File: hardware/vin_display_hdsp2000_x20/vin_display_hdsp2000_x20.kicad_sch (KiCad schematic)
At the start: 51 parts, among them J1 DEBUG, J2 USB_B_Micro, J3 DEBUG_UART, J4 IF_UART, J5 AUX_CONNECTOR, Q1 BSS138, SW1 SW_RESET, SW2 BOOTSEL, SW3 KNOB, U1 W25Q16JVSNIQ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

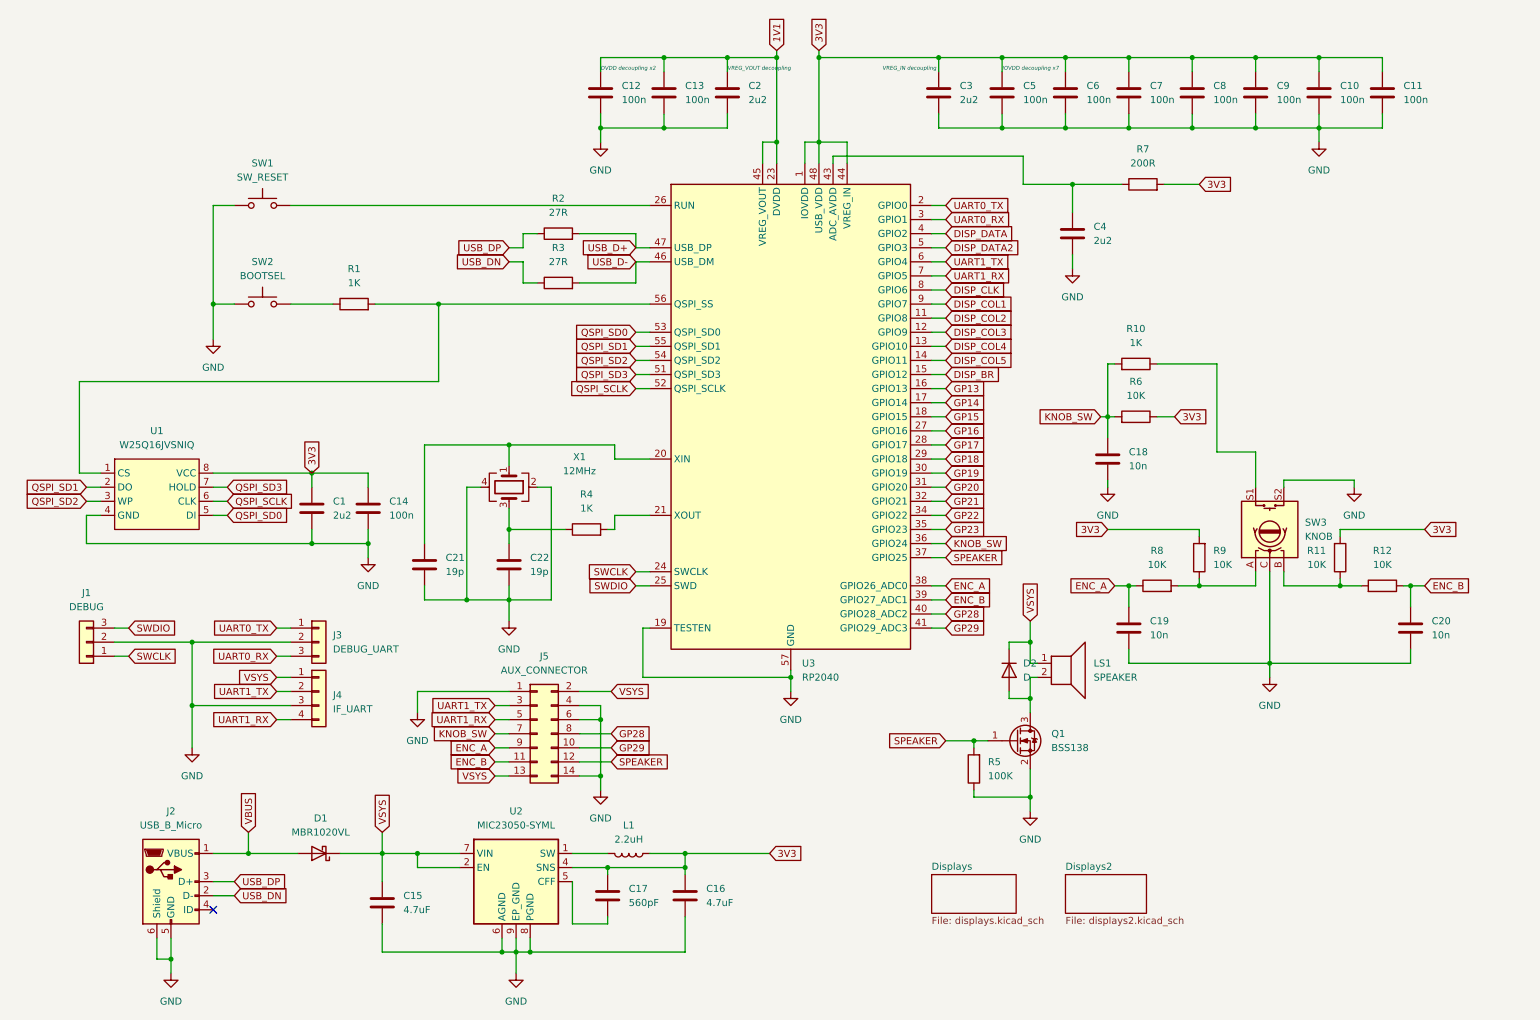
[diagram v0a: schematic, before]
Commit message: route hdsp2000_x20 board
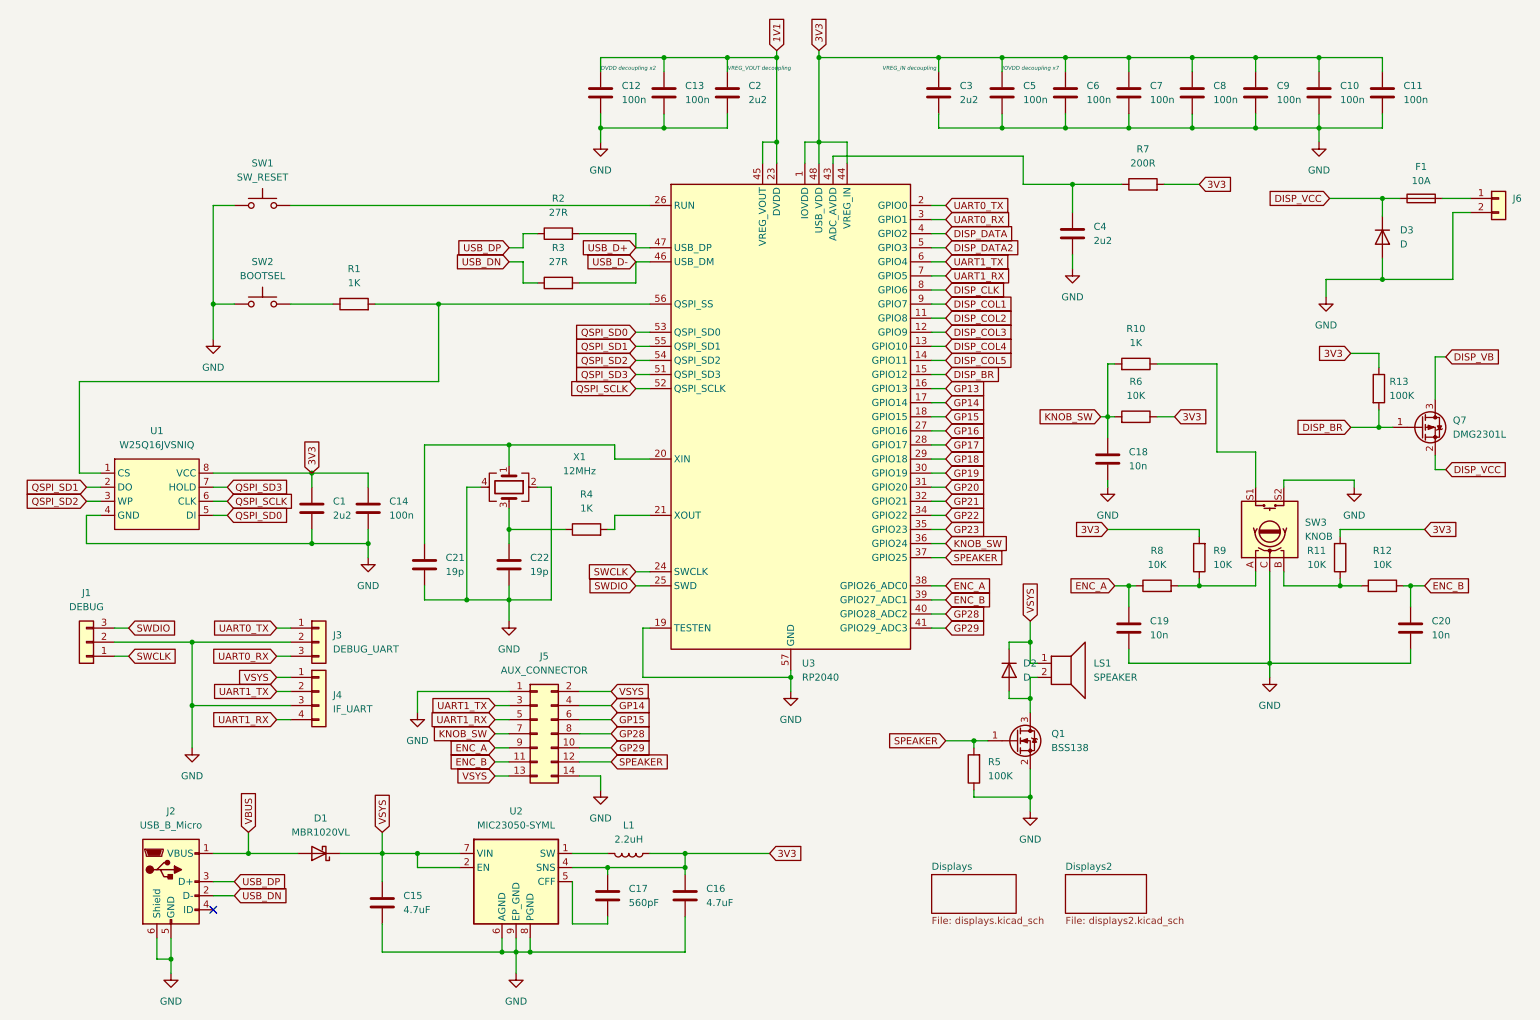
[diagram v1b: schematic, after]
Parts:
- added D3: D, components:Diode_TO252, symbol Device:D
- added F1: 10A, components:Fuse_2410, symbol Device:Fuse
- added J6: Conn_01x02, components:Conn_2x3_96, symbol Connector_Generic:Conn_01x02
- added Q7: DMG2301L, Package_TO_SOT_SMD:SOT-23, symbol Transistor_FET:DMG2301L
- added R13: 100K, Resistor_SMD:R_0603_1608Metric, symbol Device:R
- J1, J3: footprint Connector_PinHeader_2.54mm:PinHeader_1x03_P2.54mm_Vertical -> Connector_JST:JST_EH_B3B-EH-A_1x03_P2.50mm_Vertical
- J4: footprint Connector_PinHeader_2.54mm:PinHeader_1x04_P2.54mm_Vertical -> Connector_JST:JST_EH_B4B-EH-A_1x04_P2.50mm_Vertical
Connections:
- net 3V3: now also R13.1
- net DISP_BR: now also Q7.1 (G), R13.2
- net GND: now also D3.2 (A), J6.2 (Pin_2); no longer J5.4 (Pin_4), J5.6 (Pin_6)
- net GP14: now also J5.4 (Pin_4)
- net GP15: now also J5.6 (Pin_6)
- new net: F1.2, J6.1 (Pin_1)
- new net DISP_VB: Q7.3 (D)
- new net DISP_VCC: D3.1 (K), F1.1, Q7.2 (S)

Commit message: hdsp2000_x20 minor changes
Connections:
- net GP13: no longer names the net of U3.16 (GPIO13)
- net GP16: no longer names the net of U3.27 (GPIO16)
- net GP17: no longer names the net of U3.28 (GPIO17)
- net GP18: no longer names the net of U3.29 (GPIO18)
- net GP19: no longer names the net of U3.30 (GPIO19)
- net GP20: no longer names the net of U3.31 (GPIO20)
- net GP21: no longer names the net of U3.32 (GPIO21)
- net GP22: no longer names the net of U3.34 (GPIO22)
- net GP23: no longer names the net of U3.35 (GPIO23)
- no-connect marks 1 -> 10
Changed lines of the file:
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@@
   (junction (at 130.81 22.86) (diameter 0) (color 0 0 0 0)
   )
+  (no_connect (at 181.61 97.79))
+  (no_connect (at 181.61 90.17))
+  (no_connect (at 181.61 92.71))
+  (no_connect (at 181.61 82.55))
+  (no_connect (at 181.61 95.25))
+  (no_connect (at 181.61 102.87))
+  (no_connect (at 181.61 107.95))
+  (no_connect (at 181.61 100.33))
+  (no_connect (at 181.61 105.41))
   (no_connect (at 49.53 176.53))
   (wire (pts (xy 125.73 80.01) (xy 128.27 80.01))
@@
     )
   )
-  (global_label "GP20" (shape input) (at 181.61 100.33 0) (fields_autoplaced)
-    (effects (font (size 1.27 1.27)) (justify left))
-    (property "Intersheetrefs" "${INTERSHEET_REFS}" (at 189.5542 100.33 0)
-      (effects (font (size 1.27 1.27)) (justify left) hide)
-    )
-  )
   (global_label "VSYS" (shape input) (at 100.33 152.4 180) (fields_autoplaced)
     (effects (font (size 1.27 1.27)) (justify right))
@@
     )
   )
-  (global_label "GP16" (shape input) (at 181.61 90.17 0) (fields_autoplaced)
-    (effects (font (size 1.27 1.27)) (justify left))
-    (property "Intersheetrefs" "${INTERSHEET_REFS}" (at 189.5542 90.17 0)
-      (effects (font (size 1.27 1.27)) (justify left) hide)
-    )
-  )
   (global_label "KNOB_SW" (shape input) (at 181.61 110.49 0) (fields_autoplaced)
     (effects (font (size 1.27 1.27)) (justify left))
@@
     )
   )
-  (global_label "GP13" (shape input) (at 181.61 82.55 0) (fields_autoplaced)
-    (effects (font (size 1.27 1.27)) (justify left))
-    (property "Intersheetrefs" "${INTERSHEET_REFS}" (at 189.5542 82.55 0)
-      (effects (font (size 1.27 1.27)) (justify left) hide)
-    )
-  )
   (global_label "GP28" (shape input) (at 181.61 123.19 0) (fields_autoplaced)
     (effects (font (size 1.27 1.27)) (justify left))
@@
     )
   )
-  (global_label "GP19" (shape input) (at 181.61 97.79 0) (fields_autoplaced)
-    (effects (font (size 1.27 1.27)) (justify left))
-    (property "Intersheetrefs" "${INTERSHEET_REFS}" (at 189.5542 97.79 0)
-      (effects (font (size 1.27 1.27)) (justify left) hide)
-    )
-  )
   (global_label "UART1_TX" (shape input) (at 60.96 137.16 180) (fields_autoplaced)
     (effects (font (size 1.27 1.27)) (justify right))
@@
     )
   )
-  (global_label "GP22" (shape input) (at 181.61 105.41 0) (fields_autoplaced)
-    (effects (font (size 1.27 1.27)) (justify left))
-    (property "Intersheetrefs" "${INTERSHEET_REFS}" (at 189.5542 105.41 0)
-      (effects (font (size 1.27 1.27)) (justify left) hide)
-    )
-  )
   (global_label "GP14" (shape input) (at 181.61 85.09 0) (fields_autoplaced)
     (effects (font (size 1.27 1.27)) (justify left))
@@
     (effects (font (size 1.27 1.27)) (justify left))
     (property "Intersheetrefs" "${INTERSHEET_REFS}" (at 79.9306 155.5507 90)
-      (effects (font (size 1.27 1.27)) (justify left) hide)
-    )
-  )
-  (global_label "GP17" (shape input) (at 181.61 92.71 0) (fields_autoplaced)
-    (effects (font (size 1.27 1.27)) (justify left))
-    (property "Intersheetrefs" "${INTERSHEET_REFS}" (at 189.5542 92.71 0)
       (effects (font (size 1.27 1.27)) (justify left) hide)
     )
@@
     )
   )
-  (global_label "GP23" (shape input) (at 181.61 107.95 0) (fields_autoplaced)
-    (effects (font (size 1.27 1.27)) (justify left))
-    (property "Intersheetrefs" "${INTERSHEET_REFS}" (at 189.5542 107.95 0)
-      (effects (font (size 1.27 1.27)) (justify left) hide)
-    )
-  )
   (global_label "DISP_COL1" (shape input) (at 181.61 67.31 0) (fields_autoplaced)
     (effects (font (size 1.27 1.27)) (justify left))
@@
     )
   )
-  (global_label "GP21" (shape input) (at 181.61 102.87 0) (fields_autoplaced)
-    (effects (font (size 1.27 1.27)) (justify left))
-    (property "Intersheetrefs" "${INTERSHEET_REFS}" (at 189.5542 102.87 0)
-      (effects (font (size 1.27 1.27)) (justify left) hide)
-    )
-  )
   (global_label "SPEAKER" (shape input) (at 181.61 146.05 180) (fields_autoplaced)
     (effects (font (size 1.27 1.27)) (justify right))
@@
       (effects (font (size 1.27 1.27)) (justify left) hide)
     )
-  )
-  (global_label "GP18" (shape input) (at 181.61 95.25 0) (fields_autoplaced)
-    (effects (font (size 1.27 1.27)) (justify left))
-    (property "Intersheetrefs" "${INTERSHEET_REFS}" (at 189.5542 95.25 0)
-      (effects (font (size 1.27 1.27)) (justify left) hide)
-    )
